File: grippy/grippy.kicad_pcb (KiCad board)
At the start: 2 copper layers, 57.7 x 37.1 mm, 9 parts, among them J1 Conn_01x08_Socket, SW0 SW_SPST, SW1 SW_SPST, SW2 SW_SPST, SW3 SW_SPST, SW4 SW_SPST, SW5 SW_DPDT_x2, U1 esp32s3-supermini

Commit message: got a board
ready to burn
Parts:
- moved BAT1 11.5 mm to (177.1, 98.8), turned to 45 degrees
- moved SW5 7.80 mm to (174.6, 88.8)
- moved SW3 7.60 mm to (232.9, 70.8)
- moved SW2 5.65 mm to (215.9, 70.8)
- moved U1 5.53 mm to (224.2, 86.7)
- moved J1 4.64 mm to (206.3, 86.2), turned to 0 degrees
- moved SW1 2.93 mm to (196.6, 70.8)
- moved SW0 0.90 mm to (179.6, 70.8)
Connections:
- SW5 pad 1: /B+ -> /RAW
- SW5 pad 2: /RAW -> /B+
- U1 pad IO10: /DC -> /RES
- U1 pad IO11: /RES -> /DC
- U1 pad IO12: /SDA -> /CS
- U1 pad IO13: /SCL -> /BLK
- U1 pad IO8: /BLK -> /SCL
- U1 pad IO9: /CS -> /SDA
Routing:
- net /BLK: track 0.00 -> 50.7 mm
- net /CS: track 0.00 -> 50.3 mm
- net /DC: track 0.00 -> 43.5 mm
- net /RES: track 0.00 -> 43.2 mm
- net /SDA: track 0.00 -> 36.3 mm
- net /SCL: track 0.00 -> 36.0 mm
- net VCC: track 25.4 -> 53.9 mm
- net /RAW: track 55.2 -> 82.5 mm
- net GND: track 23.9 -> 0.00 mm
- net /pinky: track 16.1 -> 24.4 mm
- net /index: track 39.4 -> 44.5 mm
- net /thumb: track 43.5 -> 48.6 mm
- net /mp: track 4.95 -> 0.00 mm
- net /middle: track 26.1 -> 30.0 mm
- net /B+: track 6.68 -> 10.3 mm
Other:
- board size 57.7 x 37.1 mm -> 66.1 x 35.4 mm
- board text added: "20250903"
- board text added: "GriPPy"
- board text removed: "20250902"
- board text removed: "grippy"

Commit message: milled, stencil
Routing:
- net /mp: track 0.00 -> 4.95 mm
- net /pinky: track 24.4 -> 19.9 mm
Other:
- outline, holes or cut-outs redrawn

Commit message: got a fairly usable case
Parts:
- moved BAT1 30.3 mm to (207.4, 97.2), turned to -90 degrees
- moved SW5 2.21 mm to (174.6, 91.0)
- moved U1 1.28 mm to (224.2, 85.4)
- moved J1 1.08 mm to (205.4, 85.5)
- moved SW0 0.47 mm to (179.1, 70.8)
- moved SW1 0.47 mm to (196.2, 70.8)
- moved SW2 0.47 mm to (215.4, 70.8)
- moved SW3 0.47 mm to (232.4, 70.8)
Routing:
- net /B+: track 10.3 -> 34.5 mm
- net /mp: track 4.95 -> 13.5 mm
- net /RAW: track 82.4 -> 73.9 mm
- net VCC: track 54.0 -> 49.1 mm
- net /BLK: track 50.7 -> 52.5 mm
- net /DC: track 43.5 -> 44.6 mm
- net /pinky: track 19.9 -> 18.9 mm
- net /ring: track 15.9 -> 14.9 mm
- net /CS: track 50.3 -> 51.0 mm
- net /thumb: track 48.1 -> 47.4 mm
- net /SDA: track 36.3 -> 37.0 mm
- net /middle: track 30.5 -> 29.9 mm
- net /index: track 44.7 -> 44.2 mm
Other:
- board size 66.1 x 35.4 mm -> 64.1 x 33 mm
- board text added: "20250905"
- board text removed: "20250903"

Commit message: bumped the size up
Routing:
- net /CS: track 51.0 -> 52.4 mm
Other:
- board text added: "20250910"
- board text removed: "20250905"

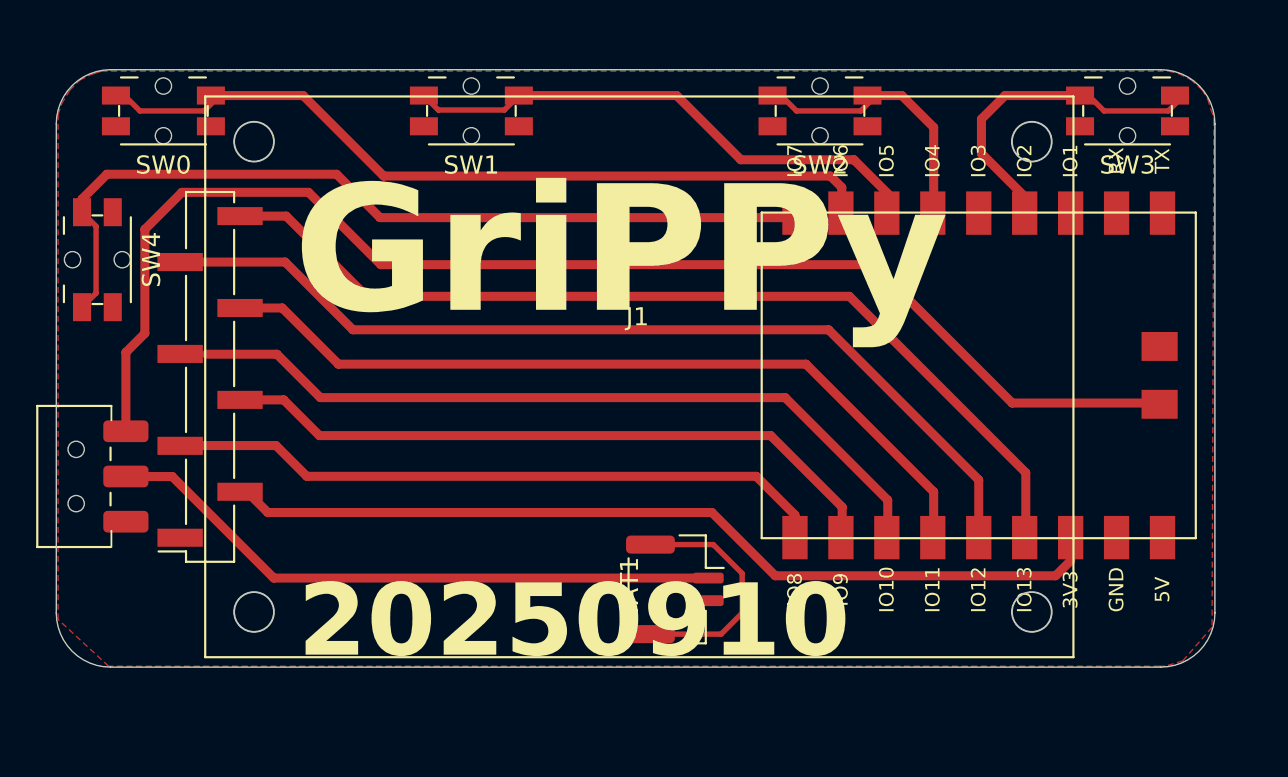
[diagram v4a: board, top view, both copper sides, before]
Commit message: new design
shorter, thicker with big fat pink buttons. plenty of room for a 150mA battery.
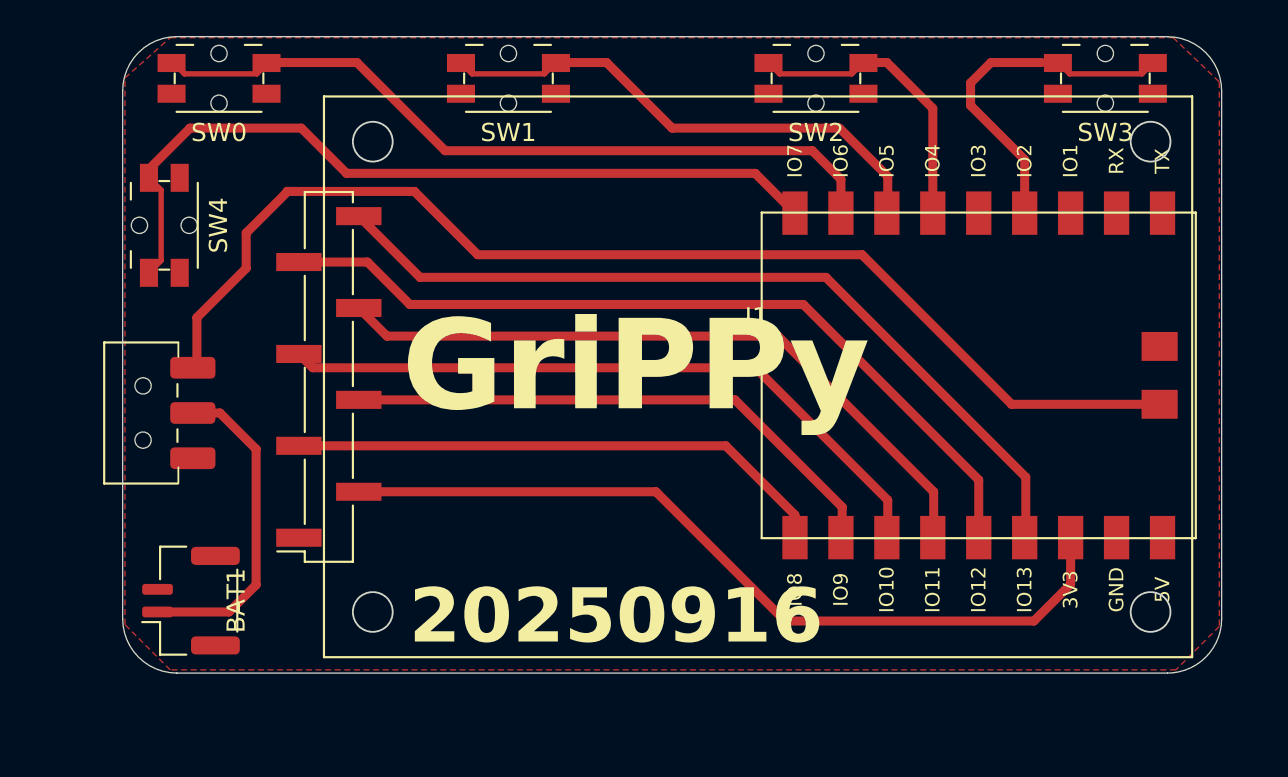
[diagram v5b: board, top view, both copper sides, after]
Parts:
- moved BAT1 26.8 mm to (180.7, 97.9), turned to 90 degrees
- moved J1 6.56 mm to (212.0, 85.5)
- moved SW5 5.10 mm to (178.2, 87.5)
- moved SW4 4.16 mm to (179.2, 77.1)
- moved SW0 3.56 mm to (182.2, 69.0)
- moved SW1 2.73 mm to (198.2, 69.0)
- moved SW3 2.18 mm to (231.2, 69.0)
- moved SW2 1.81 mm to (215.2, 69.0)
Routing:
- net /B+: track 34.5 -> 17.2 mm
- net /mp: track 13.5 -> 0.00 mm
- net /RAW: track 73.8 -> 65.0 mm
- net /BLK: track 52.5 -> 46.5 mm
- net /CS: track 52.4 -> 46.5 mm
- net /SCL: track 36.4 -> 30.5 mm
- net /SDA: track 37.0 -> 31.2 mm
- net /DC: track 44.6 -> 38.8 mm
- net /RES: track 43.4 -> 38.3 mm
- net VCC: track 49.1 -> 45.7 mm
- net /thumb: track 47.6 -> 45.4 mm
- net /index: track 44.2 -> 42.1 mm
- net /ring: track 14.9 -> 16.4 mm
- net /middle: track 29.9 -> 29.1 mm
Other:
- board size 64.1 x 33 mm -> 60.8 x 35.2 mm
- board text added: "20250916"
- board text removed: "20250910"
